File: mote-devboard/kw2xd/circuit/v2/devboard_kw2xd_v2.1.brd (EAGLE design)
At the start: 41.6 x 55.9 mm, 21 parts, among them J1 CORTEX_DEBUG_PTH, Q1 RED, Q2 RED, Q3 GREEN

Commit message: WIP
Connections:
- removed net PTA1: PORT_A.2
- net PTA1_TDI: now also PORT_A.2
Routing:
- net PTA3_SWDIO: track 44.8 -> 87.2 mm, vias 2 -> 5
- net PTA1_TDI: track 0.00 -> 39.2 mm, vias 0 -> 5
- net GND: track 214.3 -> 185.1 mm, vias 1 -> 5
- net PTE19: track 31.3 -> 57.3 mm, vias 0 -> 2
- net VCC: track 117.2 -> 95.0 mm, vias 0 -> 1
- net PTA0_SWDCLK: track 33.6 -> 48.9 mm, vias 1 -> 4
- net PTA18: track 17.1 -> 28.5 mm, vias 1 -> 4
- net PTA2_SWO: track 24.9 -> 21.6 mm, vias 0 -> 2
- net PTE18: track 55.6 -> 53.0 mm, vias 1 -> 3
- net PTD1: track 35.0 -> 32.6 mm
- net PTC4: track 17.2 -> 18.7 mm
- net PTE0: track 11.2 -> 12.6 mm
- net NRST: track 71.1 -> 72.2 mm, vias 5 -> 4
- net PTC5: track 15.8 -> 16.4 mm, vias 0 -> 3
- net PTE1: track 10.4 -> 11.0 mm
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
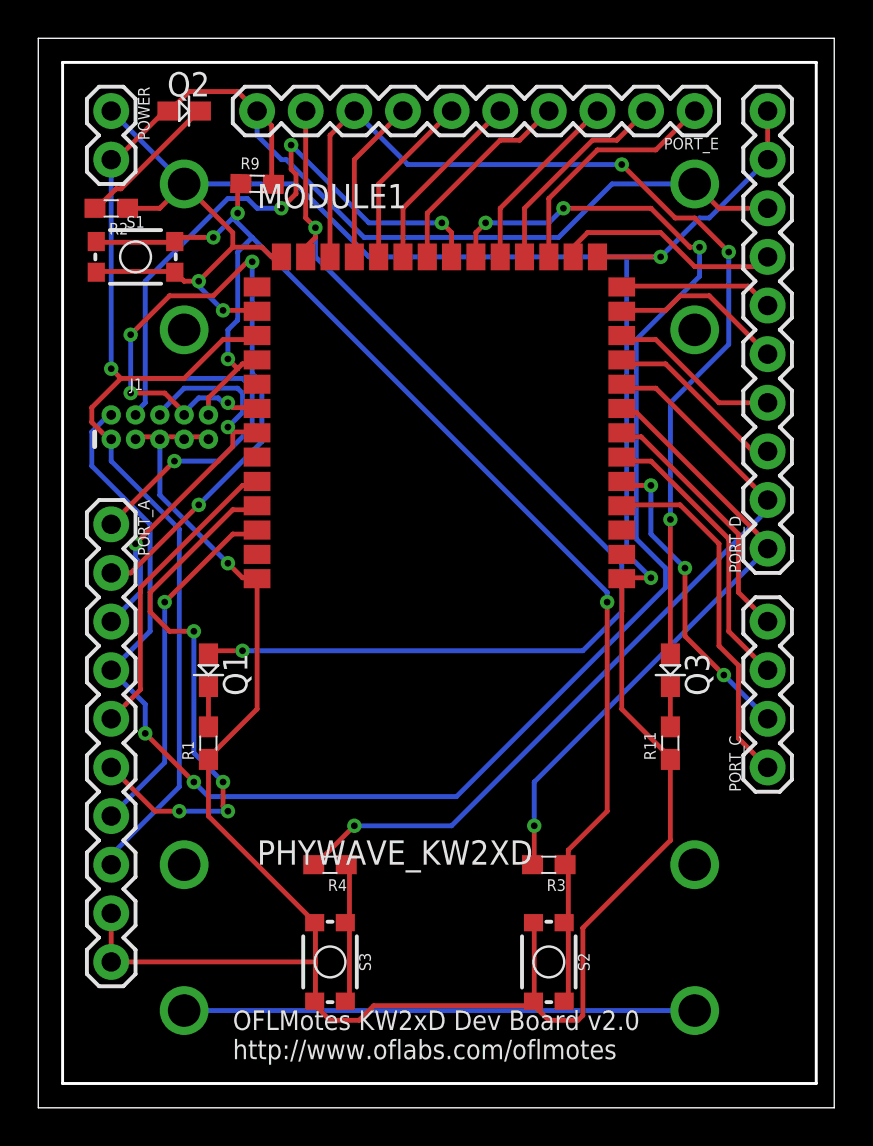
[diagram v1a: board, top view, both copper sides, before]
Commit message: 2-pin header (upper left) will be used as power switch/current meter
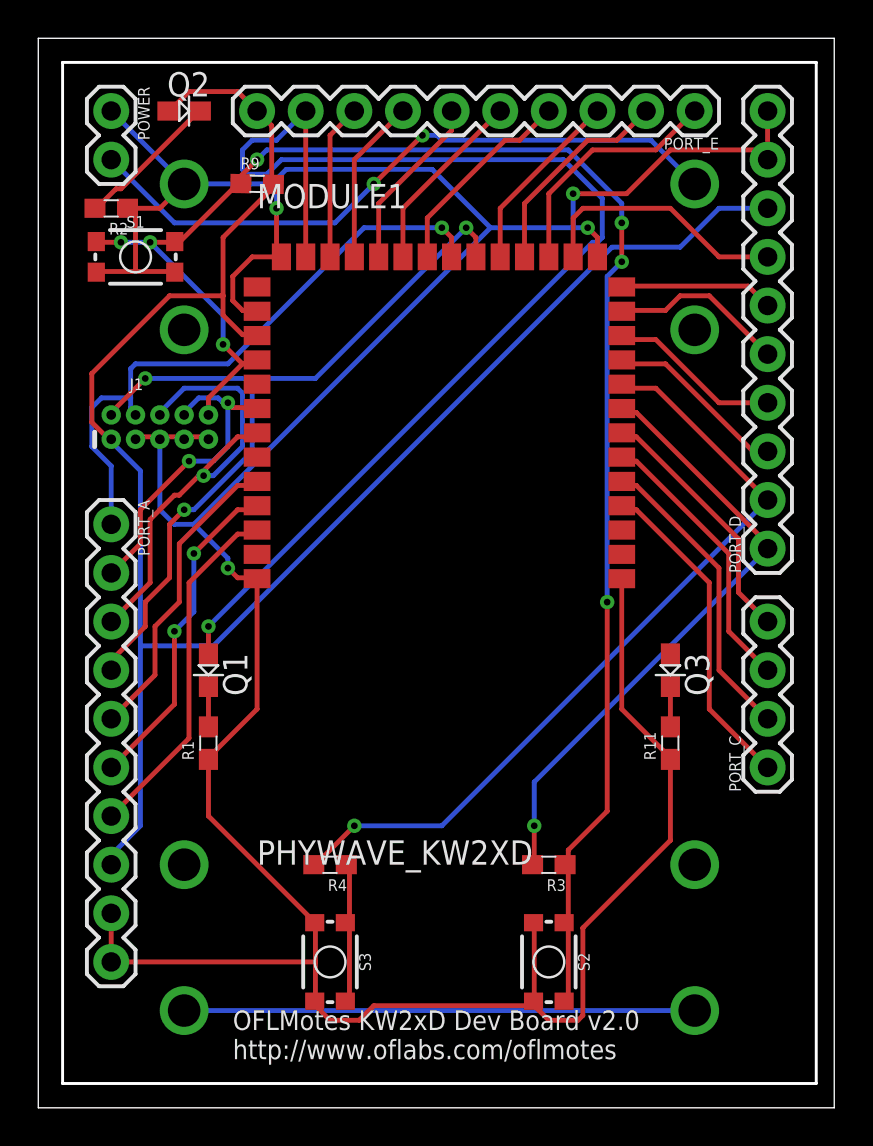
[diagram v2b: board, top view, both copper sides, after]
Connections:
- new net VBAT: BT1.PWR@1, POWER.2
- net VCC: no longer BT1.PWR@1, POWER.2
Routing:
- net PTE18: track 53.0 -> 8.15 mm, vias 3 -> 0
- net PTA3_SWDIO: track 87.2 -> 43.0 mm, vias 5 -> 3
- net VBAT: track 0.00 -> 34.8 mm, vias 0 -> 2
- net PTA1_TDI: track 39.2 -> 16.7 mm, vias 5 -> 2
- net PTA0_SWDCLK: track 48.9 -> 32.3 mm, vias 4 -> 1
- net NRST: track 72.2 -> 87.2 mm, vias 4 -> 7
- net PTA18: track 28.5 -> 17.4 mm, vias 4 -> 2
- net PTE19: track 57.3 -> 65.3 mm, vias 2 -> 1
- net VCC: track 95.0 -> 98.1 mm, vias 1 -> 0
- net PTA2_SWO: track 21.6 -> 24.5 mm, vias 2 -> 1
- net GND: track 185.1 -> 186.9 mm, vias 5 -> 4
- net PTD7: track 11.9 -> 13.5 mm
- net PTC4: track 18.7 -> 17.3 mm
- net PTC5: track 16.4 -> 16.0 mm, vias 3 -> 0
- net PTA19: track 18.8 -> 18.7 mm, vias 1 -> 0
